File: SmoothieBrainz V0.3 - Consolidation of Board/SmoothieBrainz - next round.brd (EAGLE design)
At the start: 101 x 101 mm, 222 parts, among them IC1 LPC1769, IC5 LD117ADT33TR, Q1 BSL207SP, Q2 12MHz, SW1 SW_TACT_4P_B, SW3 SW_TACT_4P_B, U3 USD-SOCKETUSD, X1 MSTBA2, X14 USBPTH, X2 GMSTBA2, X3 GMSTBA4, X4 1751248, X5 1751248, X6 1751248, X7 1751248

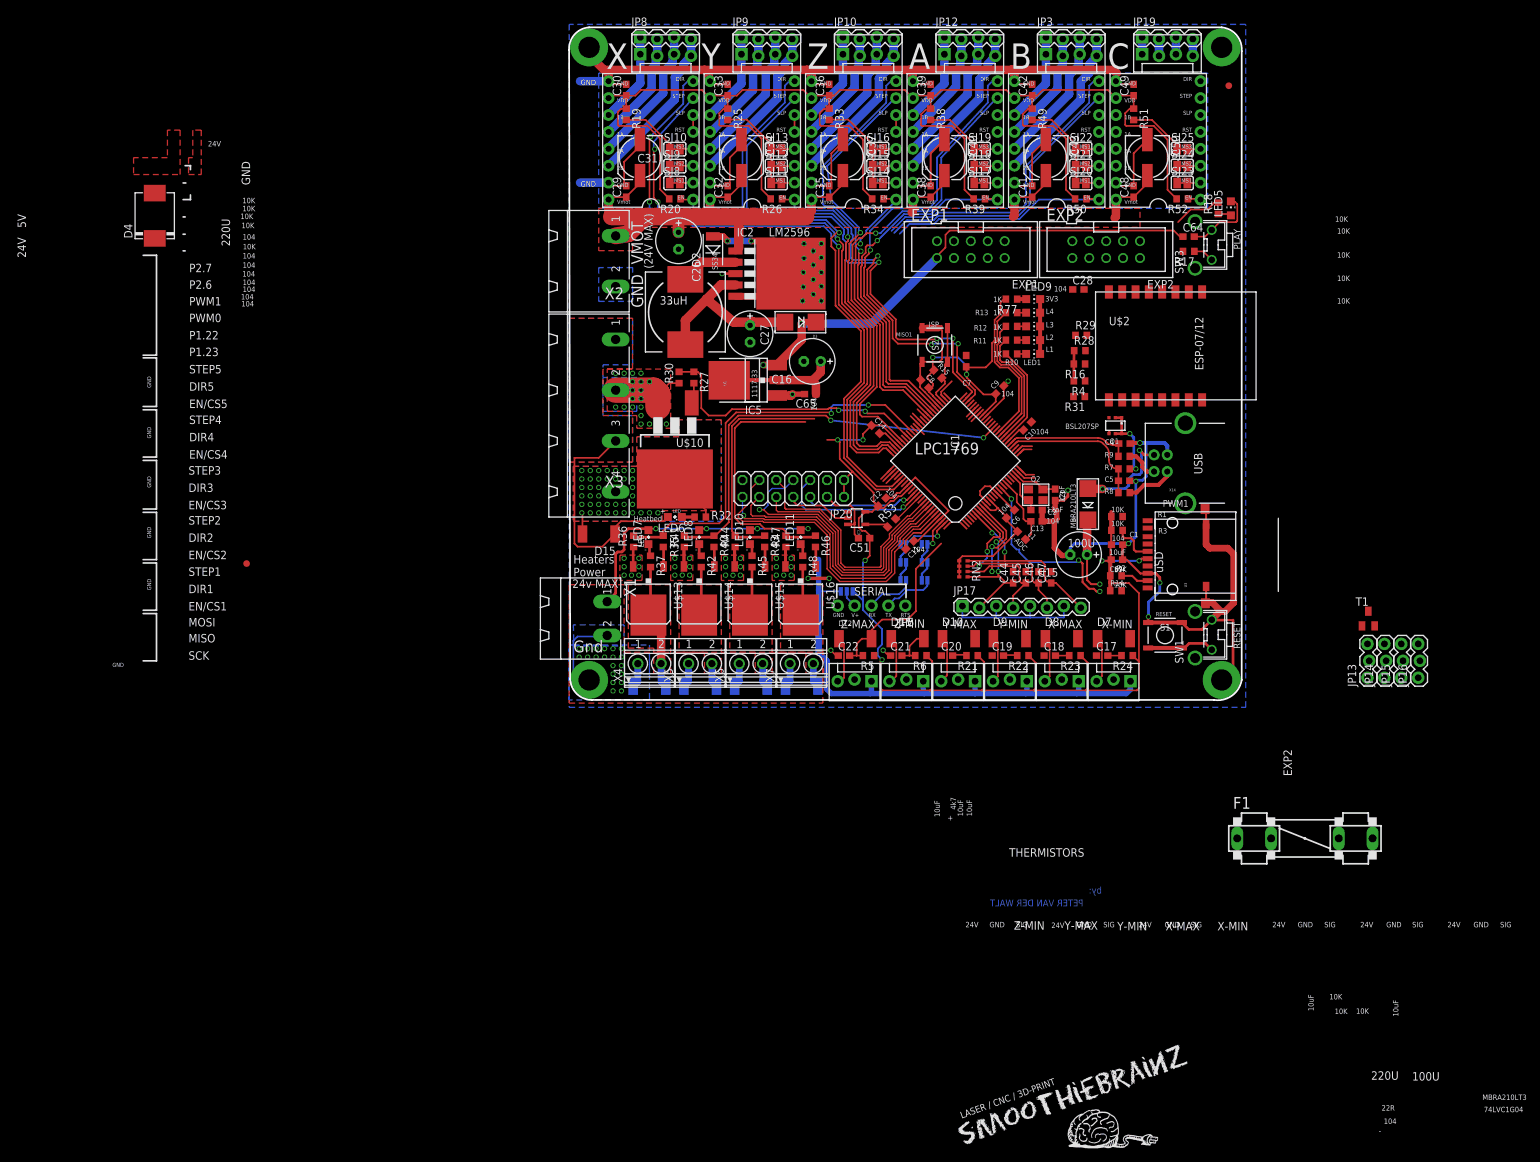
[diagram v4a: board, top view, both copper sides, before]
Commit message: ran autorouter for research purposes
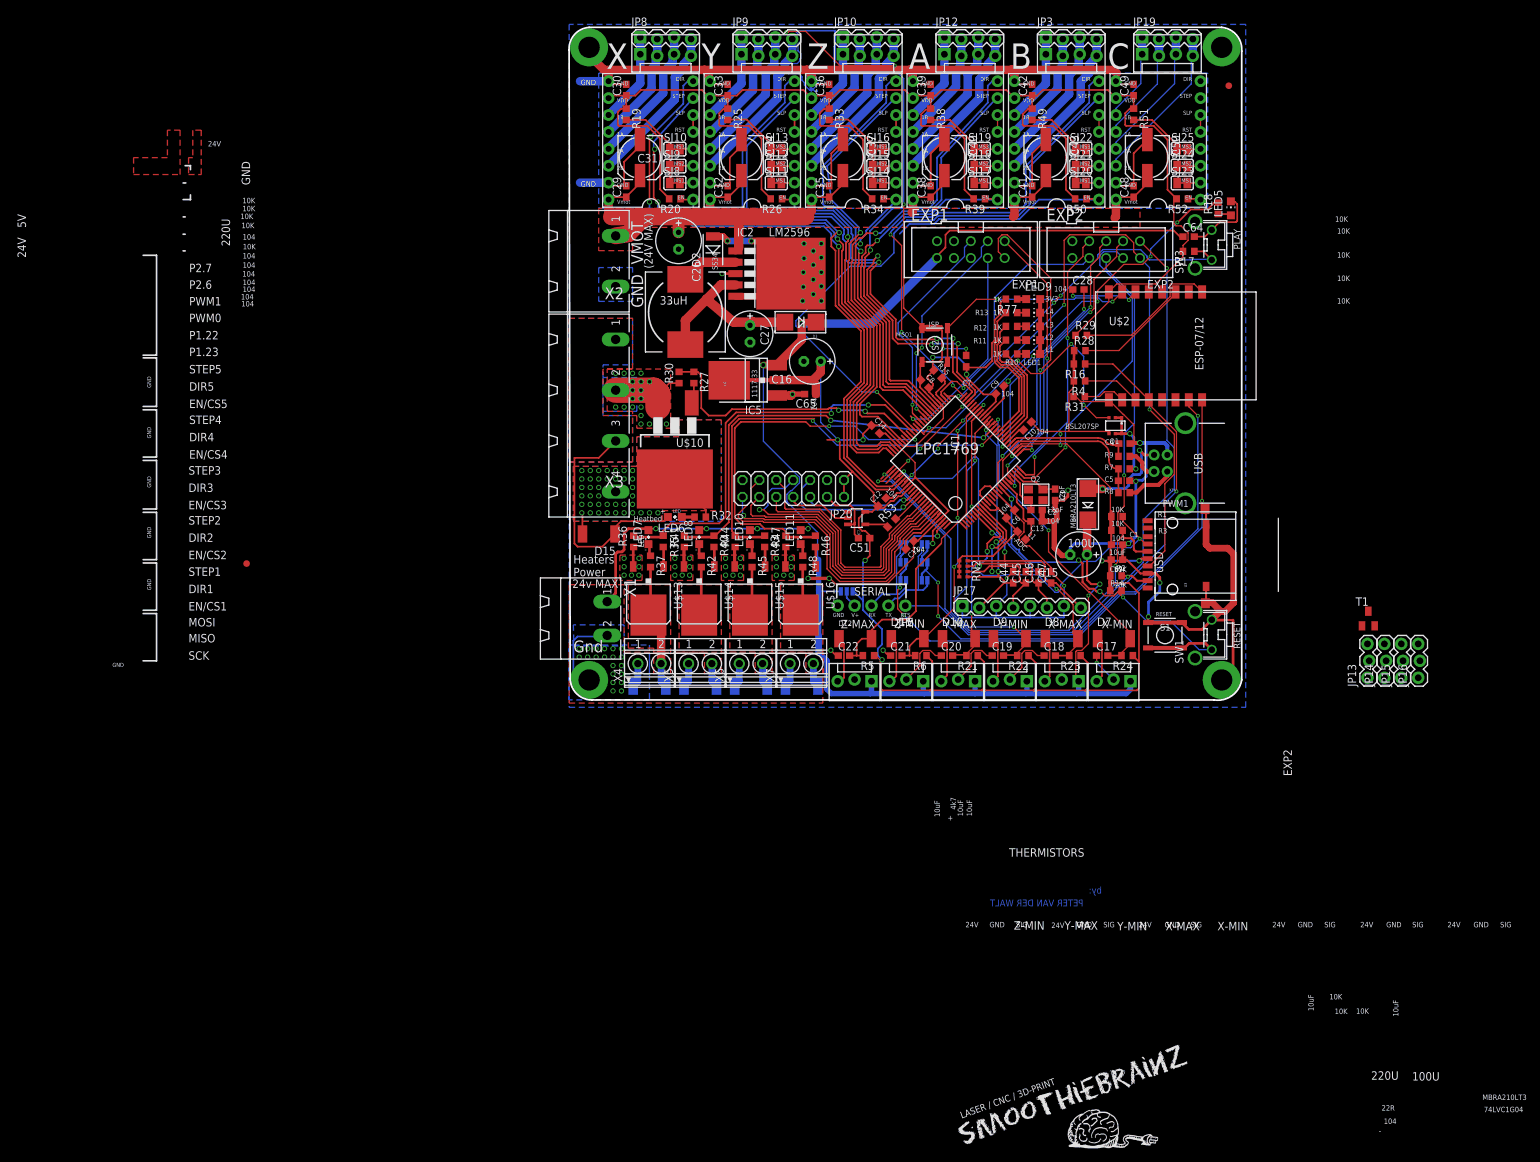
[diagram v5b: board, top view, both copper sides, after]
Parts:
- removed D4: SS34, Fairchild Rectifier Diodes s3x_10:DO214AB
- removed F1: (no value), keystone:FH_5X20
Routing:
- net GND: track 496.5 -> 698.5 mm, vias 82 -> 90
- net 3.3V: track 480.2 -> 598.4 mm, vias 8 -> 10
- net SD_MISO: track 6.31 -> 119.6 mm, vias 0 -> 3
- net SD_SCK: track 1.96 -> 111.7 mm, vias 0 -> 5
- net SD_MOSI: track 8.44 -> 113.9 mm, vias 0 -> 3
- net RTS: track 0.00 -> 82.3 mm, vias 0 -> 1
- net ESPTX: track 3.04 -> 81.4 mm, vias 0 -> 3
- net ESPRX: track 3.04 -> 78.0 mm, vias 0 -> 3
- net SD_CS: track 0.00 -> 66.9 mm, vias 0 -> 2
- net PLAY_LED: track 7.24 -> 66.5 mm, vias 0 -> 6
- net RESET: track 37.6 -> 94.5 mm, vias 3 -> 6
- net 5V: track 168.3 -> 219.4 mm, vias 3 -> 4
- net PLAY: track 3.14 -> 53.2 mm, vias 0 -> 3
- net P1_30_CLICK-ON-RRD: track 0.00 -> 47.1 mm, vias 0 -> 2
- net STP5: track 42.5 -> 89.4 mm, vias 0 -> 1
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
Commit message: reverted from auto
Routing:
- net GND: track 698.5 -> 496.5 mm, vias 90 -> 82
- net 3.3V: track 598.4 -> 480.2 mm, vias 10 -> 8
- net SD_MISO: track 119.6 -> 6.31 mm, vias 3 -> 0
- net SD_SCK: track 111.7 -> 1.96 mm, vias 5 -> 0
- net SD_MOSI: track 113.9 -> 8.44 mm, vias 3 -> 0
- net RTS: track 82.3 -> 0.00 mm, vias 1 -> 0
- net ESPTX: track 81.4 -> 3.04 mm, vias 3 -> 0
- net ESPRX: track 78.0 -> 3.04 mm, vias 3 -> 0
- net SD_CS: track 66.9 -> 0.00 mm, vias 2 -> 0
- net PLAY_LED: track 66.5 -> 7.24 mm, vias 6 -> 0
- net RESET: track 94.5 -> 37.6 mm, vias 6 -> 3
- net 5V: track 219.4 -> 168.3 mm, vias 4 -> 3
- net PLAY: track 53.2 -> 3.14 mm, vias 3 -> 0
- net P1_30_CLICK-ON-RRD: track 47.1 -> 0.00 mm, vias 2 -> 0
- net STP5: track 89.4 -> 42.5 mm, vias 1 -> 0
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
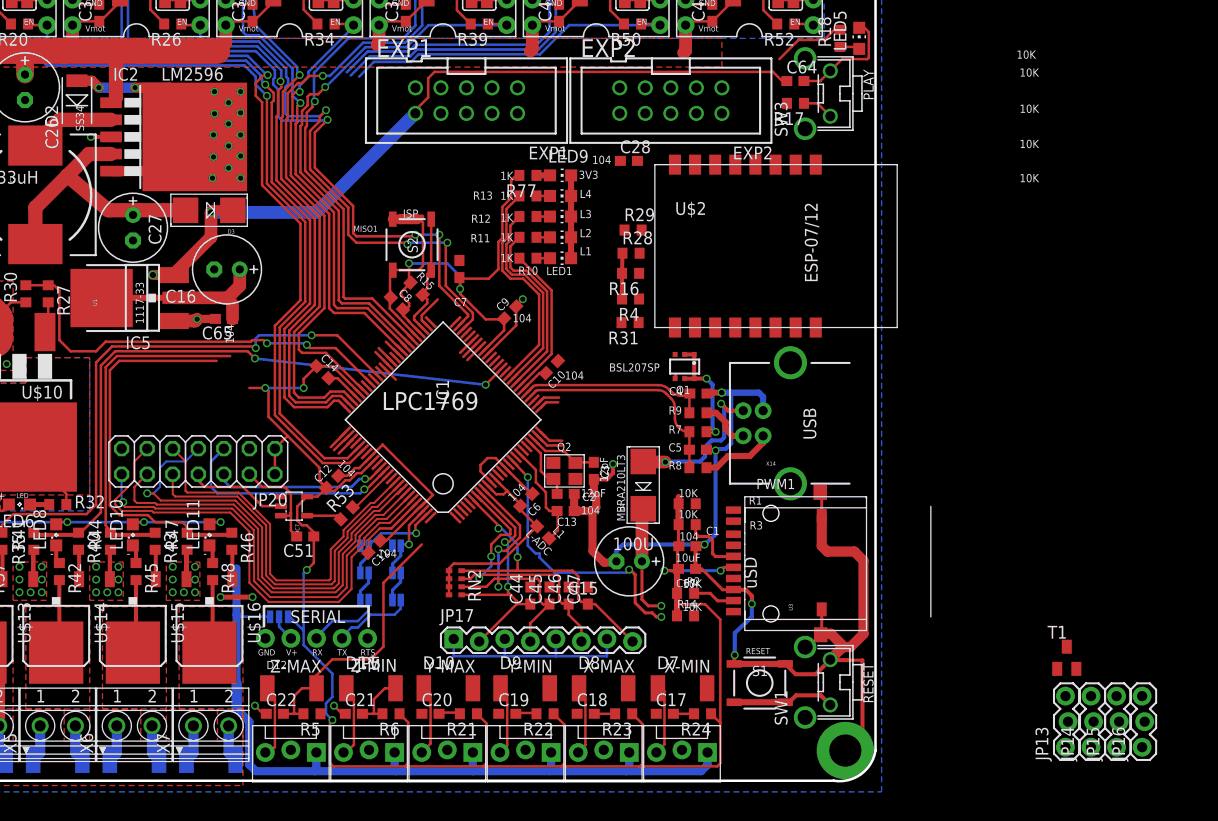
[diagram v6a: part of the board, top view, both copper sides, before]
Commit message: mosfet #6 added to board
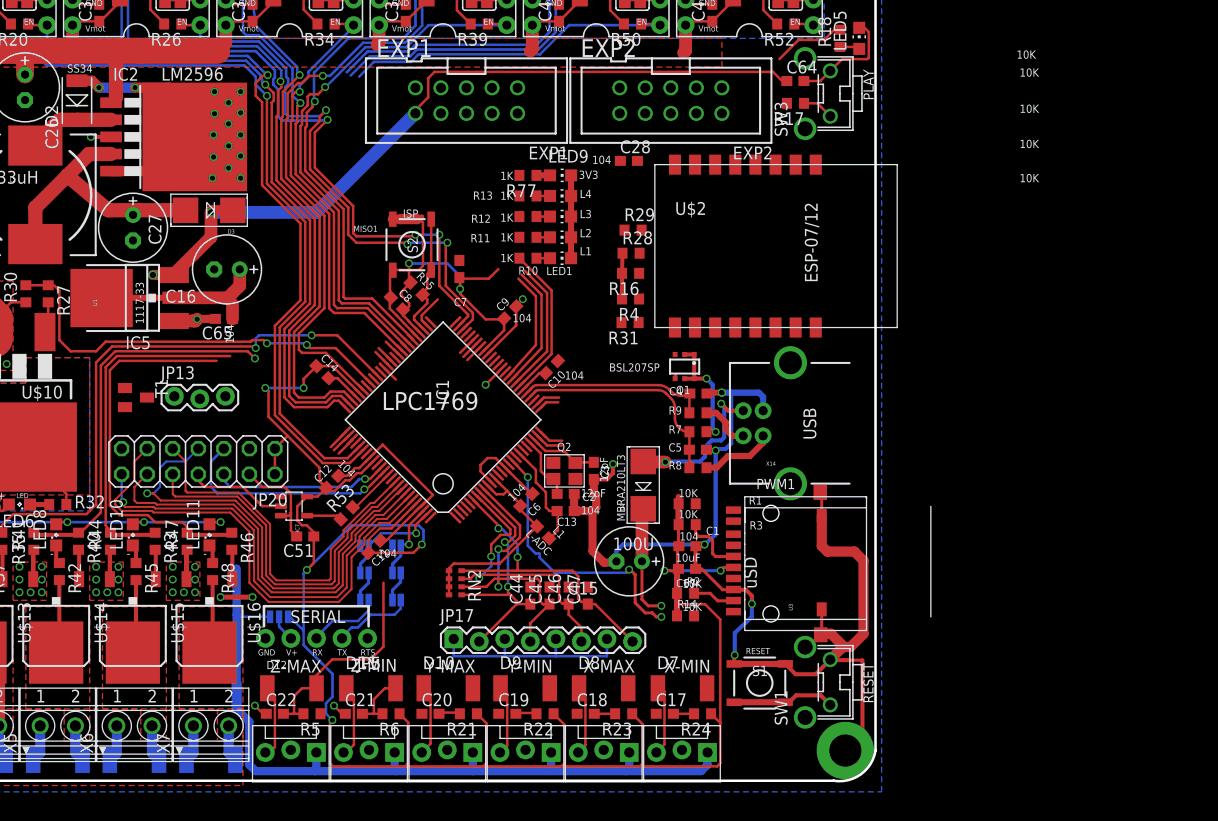
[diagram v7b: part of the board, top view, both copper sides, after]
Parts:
- removed JP14, JP15, JP16: (no value), SparkFun-Connectors:1X03_LOCK
- moved T1 96.1 mm to (27.5, 38.1), turned to 270 degrees
- moved JP13 95.3 mm to (31.3, 38.1), turned to 0 degrees
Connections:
- removed net DIR6: U$9.DIR
- removed net EN6: R52.1, U$9.EN
- removed net STP6: U$9.STEP
- net LED2: now also U$9.DIR
- net LED3: now also U$9.STEP
- net LED4: now also R52.1, U$9.EN
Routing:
- net P1_23-3RD-LARGE-FET: track 63.4 -> 40.3 mm
- net 3.3V: track 480.2 -> 489.5 mm, vias 8 -> 9
- net LED4: track 22.0 -> 13.3 mm
- net LED3: track 20.2 -> 12.3 mm
- net Z_MAX: track 29.0 -> 23.6 mm
- net LED2: track 18.3 -> 13.3 mm
- net EN6: track 1.93 -> 0.00 mm

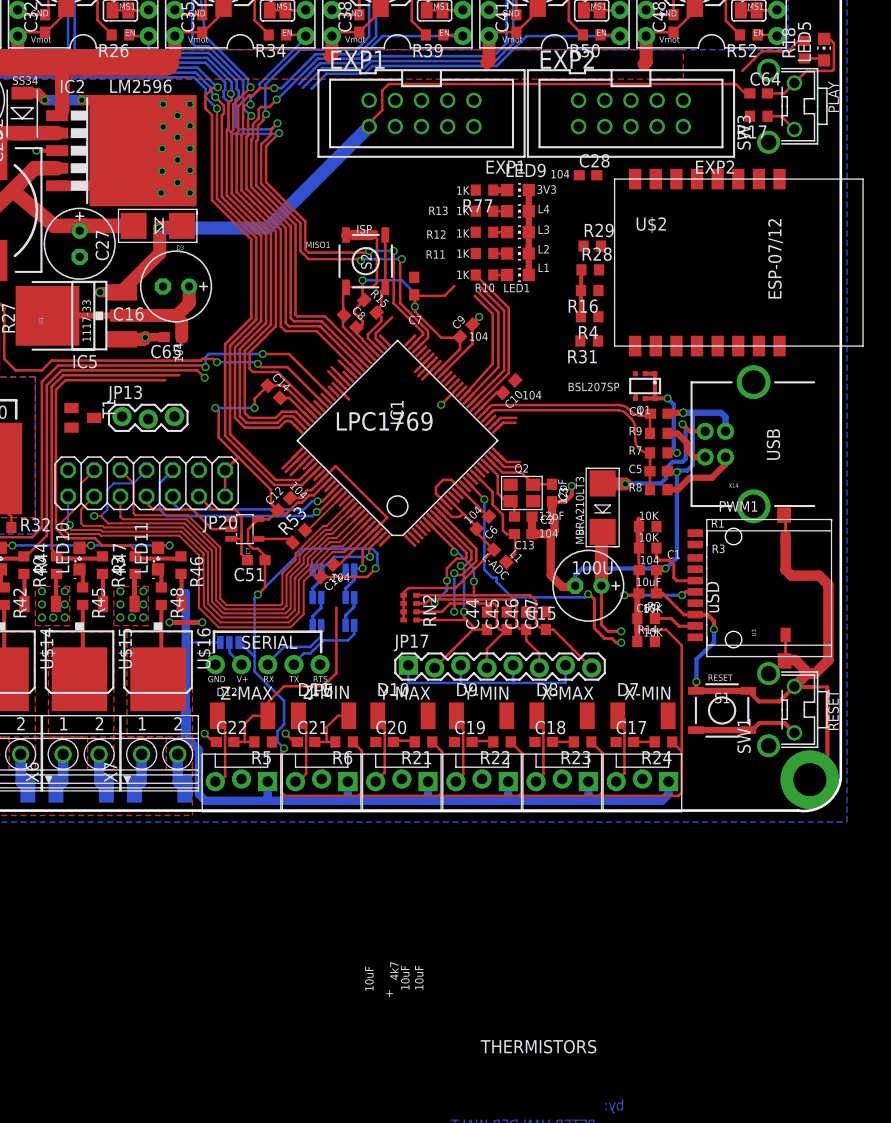
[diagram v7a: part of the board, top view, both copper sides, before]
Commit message: motor 5 routed
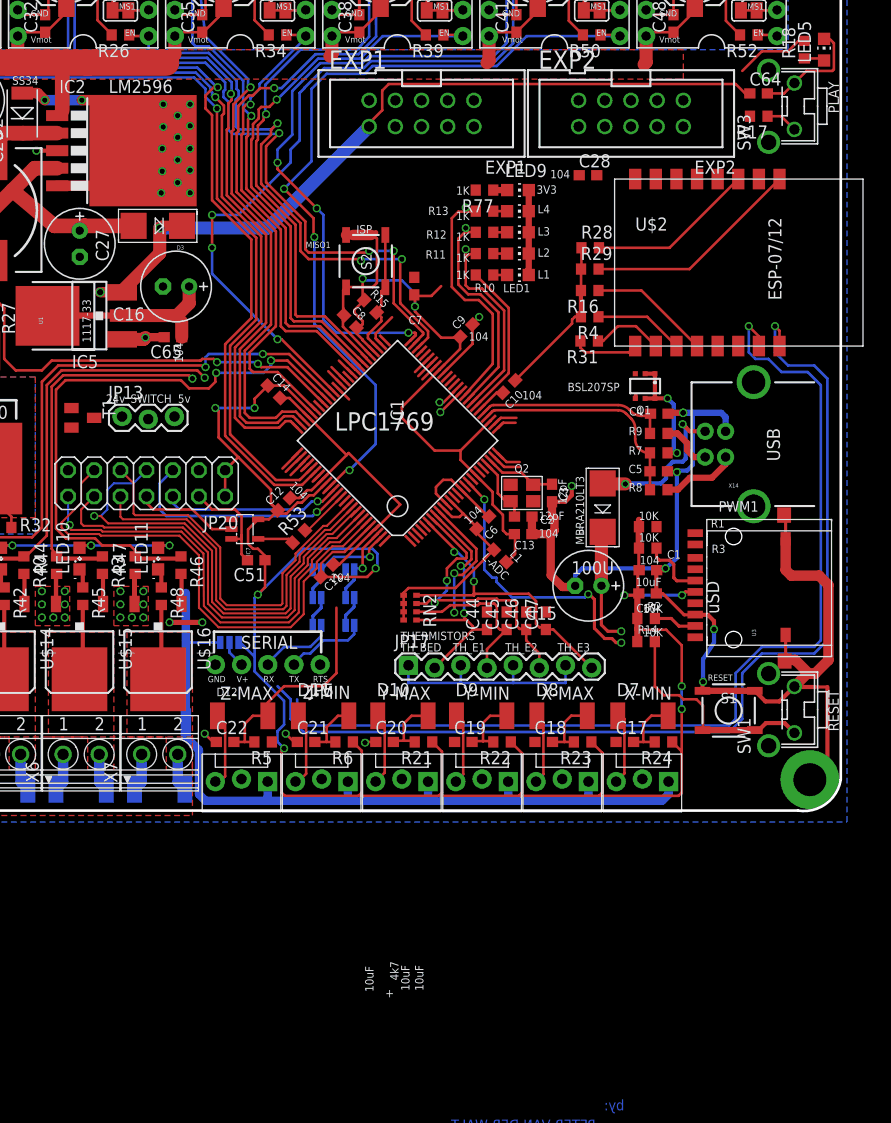
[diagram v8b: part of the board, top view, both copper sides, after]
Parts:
- moved R29 2.24 mm to (76.7, 52.5)
- moved R28 2.14 mm to (76.7, 54.6)
- moved S1 0.64 mm to (90.1, 9.71)
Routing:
- net ESPTX: track 3.04 -> 101.8 mm, vias 0 -> 1
- net ESPRX: track 3.04 -> 100.0 mm, vias 0 -> 1
- net EN5: track 34.0 -> 80.3 mm, vias 0 -> 3
- net STP5: track 42.5 -> 82.1 mm, vias 0 -> 3
- net DIR5: track 45.3 -> 81.2 mm, vias 0 -> 3
- net 3.3V: track 489.5 -> 520.1 mm, vias 9 -> 11
- net RESET1: track 0.00 -> 21.2 mm
- net P2.6_FAN_FET: track 38.3 -> 57.6 mm, vias 0 -> 2
- net N$18: track 0.00 -> 16.3 mm
- net GND: track 496.5 -> 511.6 mm, vias 82 -> 83
- net LED4: track 13.3 -> 25.6 mm, vias 0 -> 1
- net RTS: track 0.00 -> 11.8 mm
- net RESET: track 37.6 -> 49.2 mm
- net LED3: track 12.3 -> 21.3 mm, vias 0 -> 1
- net 2: track 0.00 -> 8.74 mm
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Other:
- board text added: "24v"
- board text added: "5v"
- board text added: "SWITCH"
- board text added: "TH_BED"
- board text added: "TH_E1"
- board text added: "TH_E2"
- board text added: "TH_E3"
